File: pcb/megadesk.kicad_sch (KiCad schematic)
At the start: 24 parts, among them J1 Interface, J2 FFC, J3 AVR-ISP-6, U1 L7812, U2 L7805, U3 ATtiny841-SS, U4 MCP2003B

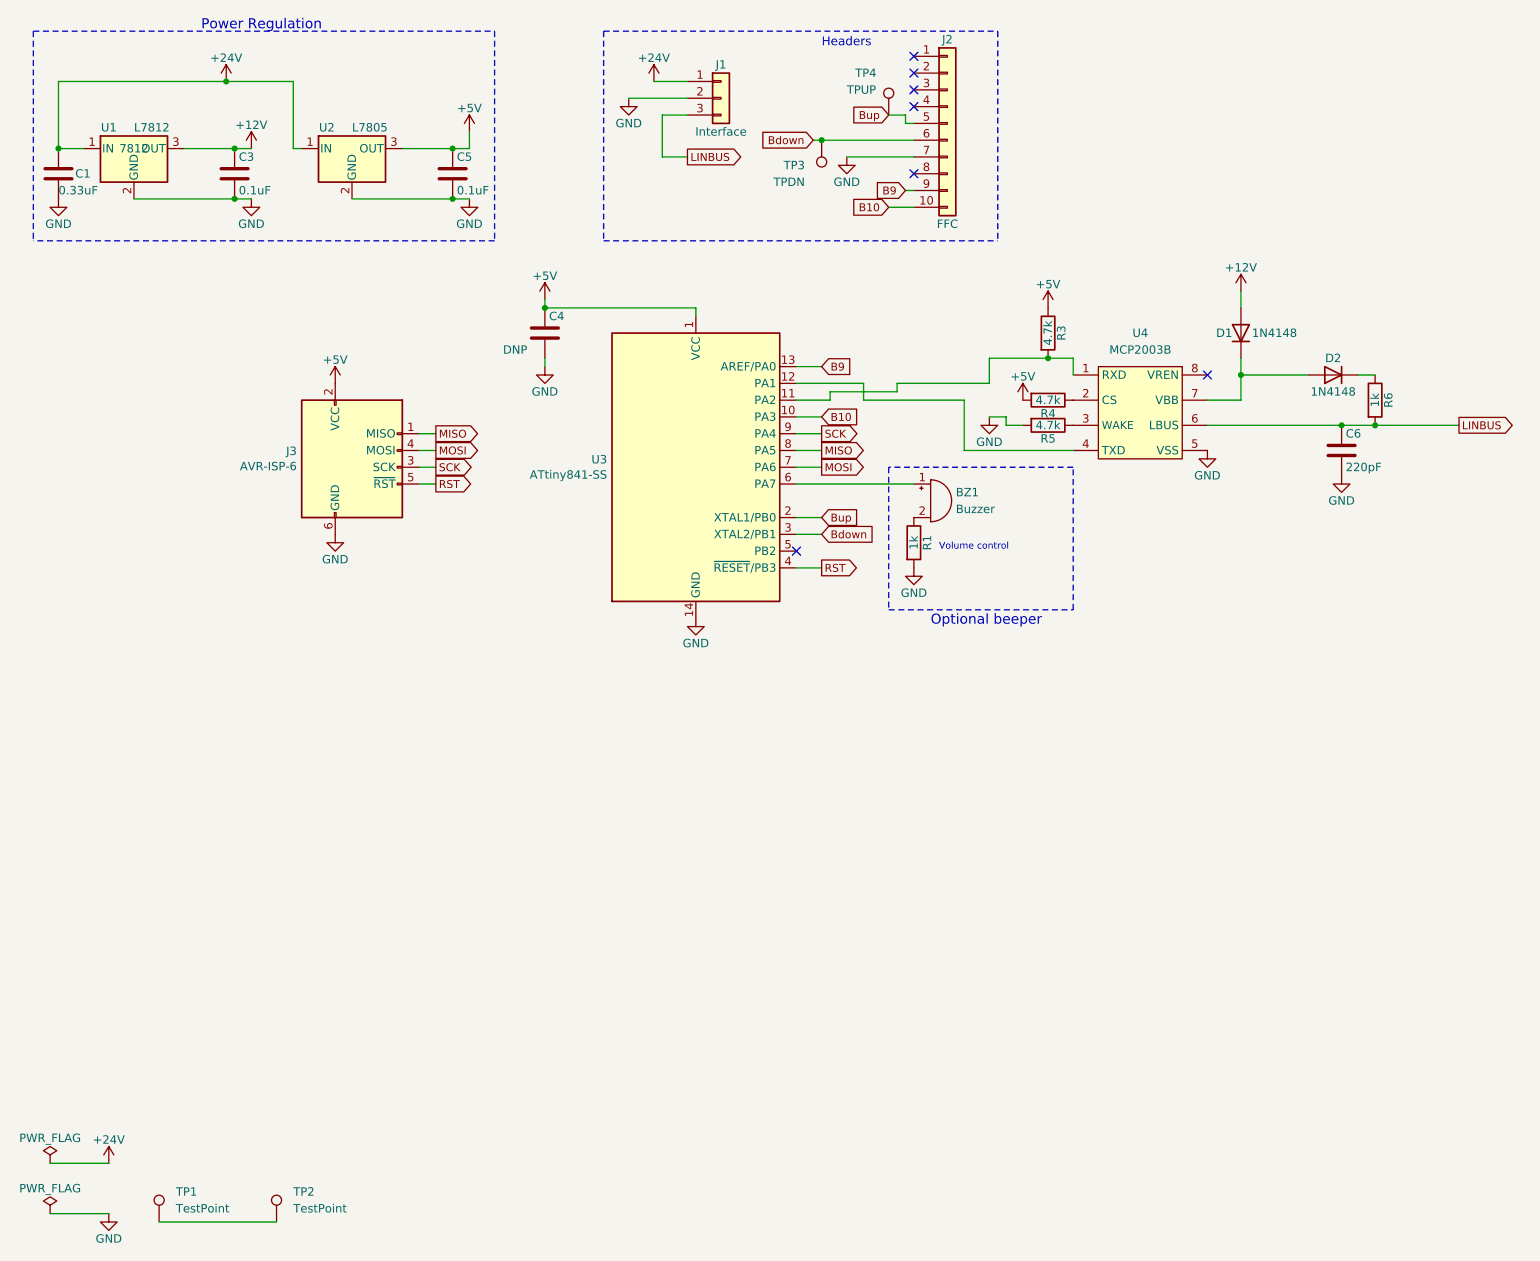
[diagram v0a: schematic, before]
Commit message: revise LDO's
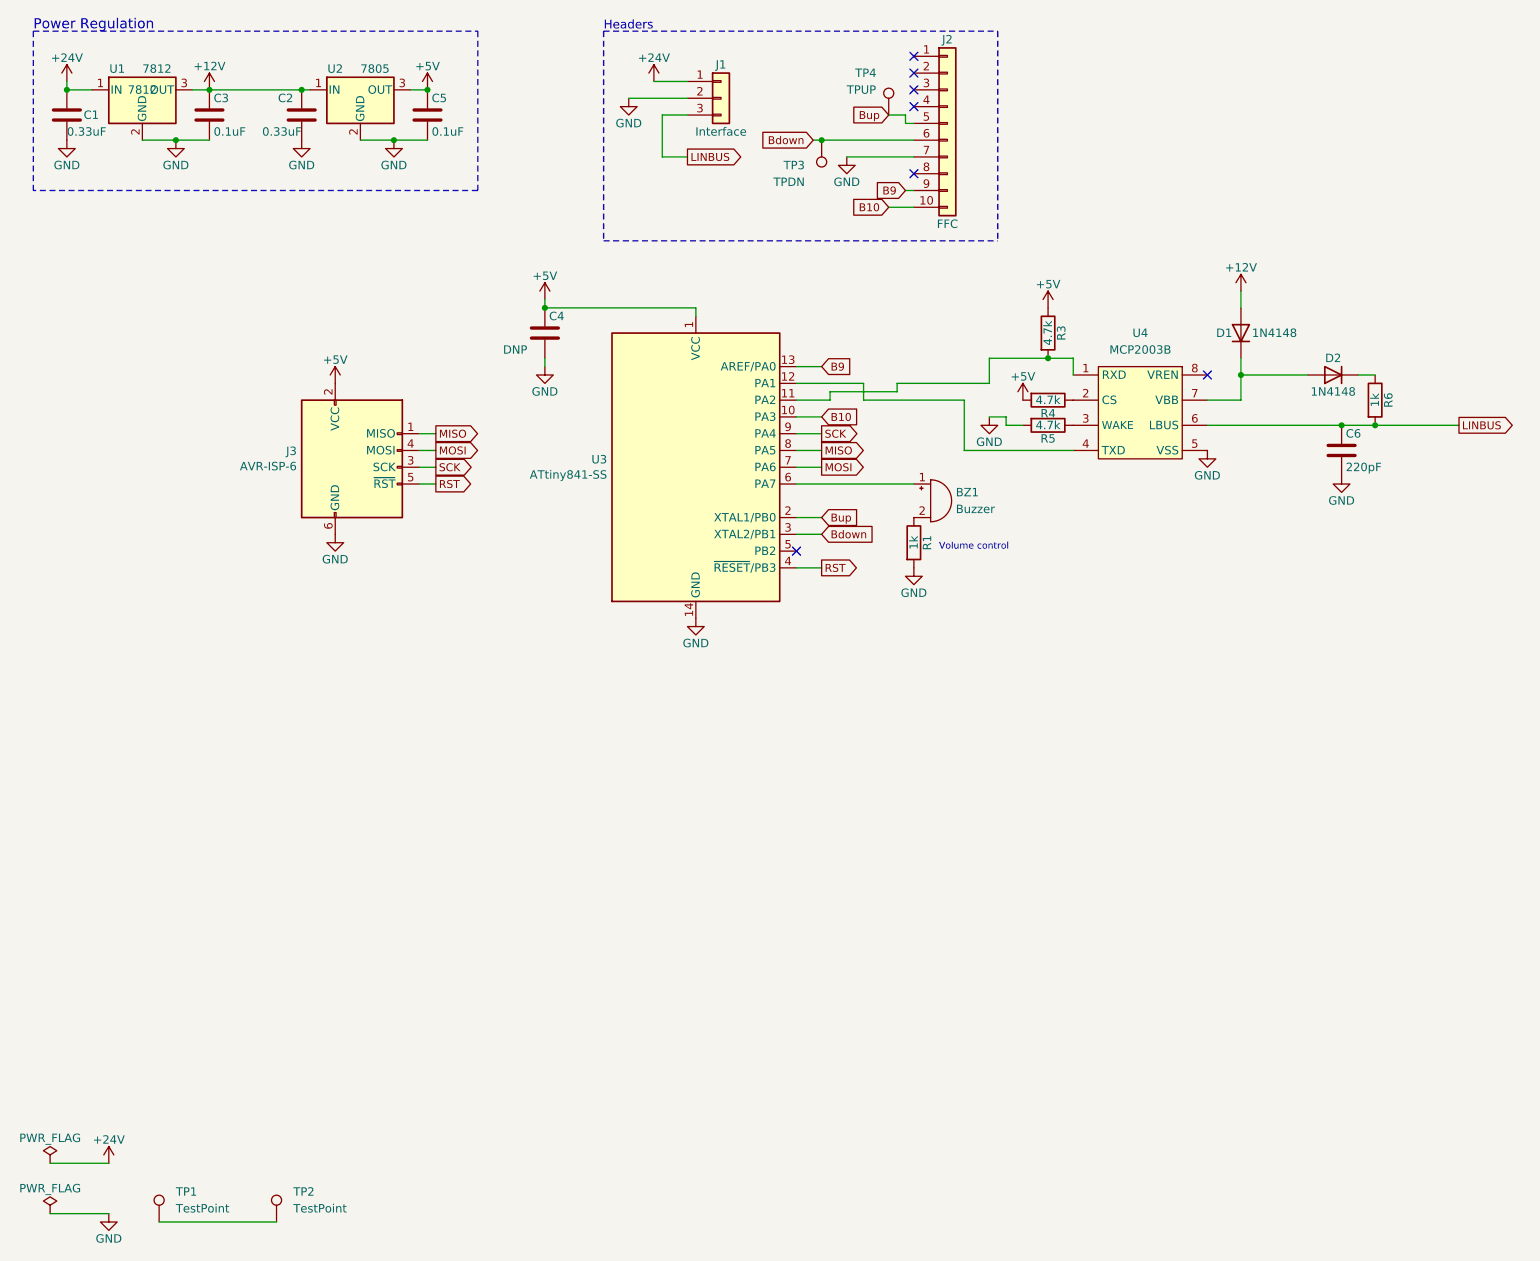
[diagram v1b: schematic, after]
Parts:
- added C2: 0.33uF, Capacitor_SMD:C_0805_2012Metric, symbol Device:C
- U1: value L7812 -> 7812; LCSC C16424 -> C116325; LCSC_ALT (none) -> C347282; Notes C16424 -> (none)
- U2: value L7805 -> 7805; footprint Package_TO_SOT_SMD:TO-252-3_TabPin2 -> Package_TO_SOT_SMD:SOT-89-3; LCSC C55509 -> C16106; Notes 35V INPUT -> (none); Part Number 7805 -> HT7550-1
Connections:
- net +12V: now also U2.1 (IN), C2.1
- net +24V: no longer U2.1 (IN)
- net GND: now also C2.2
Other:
- note removed: "Optional beeper"
- moved on the sheet: C1, C3, C5, U1, U2

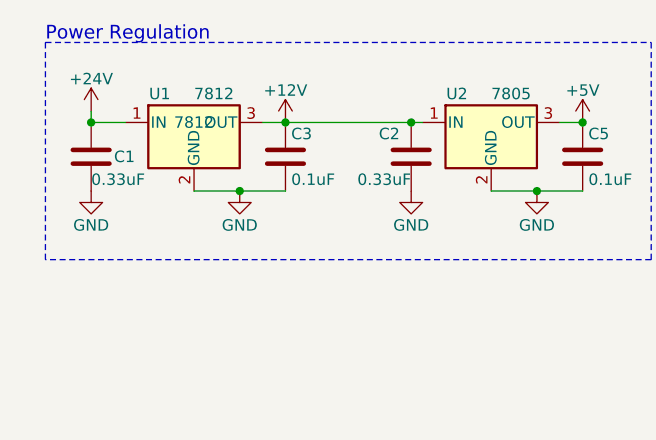
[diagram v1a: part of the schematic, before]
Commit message: simplify caps
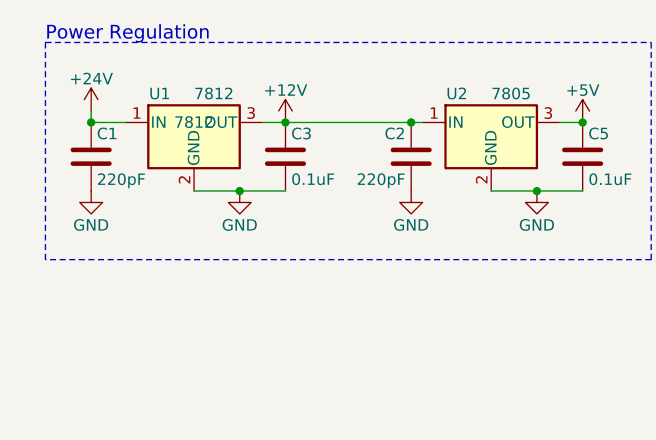
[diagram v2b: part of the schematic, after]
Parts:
- C1, C2: value 0.33uF -> 220pF; footprint Capacitor_SMD:C_0805_2012Metric -> Capacitor_SMD:C_0603_1608Metric; LCSC C1740 -> C1603

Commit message: ugh. fix bad pins.
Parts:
- removed U2: 7805, Package_TO_SOT_SMD:SOT-89-3, symbol Regulator_Linear:L7805
- added U2: HT7550-1, Package_TO_SOT_SMD:SOT-89-3, symbol Regulator_Linear:MCP1700-2502E_SOT89
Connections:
- net +12V: now also U2.2 (VI)
- net +5V: now also U2.3 (VO)
- net GND: now also U2.1 (GND)
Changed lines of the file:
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@@
     (pin "1")
-  )
-  (symbol (lib_id "Regulator_Linear:L7805") (at 64.77 26.67 0) (unit 1)
-    (in_bom yes) (on_board yes)
-    (property "Reference" "U2" (id 0) (at 60.96 23.495 0))
-    (property "Value" "7805" (id 1) (at 64.77 23.495 0)
-      (effects (font (size 1.27 1.27)) (justify left))
-    )
-    (property "Footprint" "Package_TO_SOT_SMD:SOT-89-3" (id 2) (at 65.405 30.48 0)
-      (effects (font (size 1.27 1.27) italic) (justify left) hide)
-    )
-    (property "Datasheet" "" (id 3) (at 64.77 27.94 0)
-      (effects (font (size 1.27 1.27)) hide)
-    )
-    (property "Part Number" "HT7550-1" (id 4) (at 64.77 26.67 0)
-      (effects (font (size 1.27 1.27)) hide)
-    )
-    (property "LCSC" "C16106" (id 5) (at 64.77 26.67 0)
-      (effects (font (size 1.27 1.27)) hide)
-    )
-    (property "Notes" "" (id 6) (at 64.77 26.67 0)
-      (effects (font (size 1.27 1.27)) hide)
-    )
-    (pin "1")
-    (pin "2")
-    (pin "3")
   )
   (symbol (lib_id "power:GND") (at 69.85 34.29 0) (unit 1)
@@
     (pin "1")
   )
+  (symbol (lib_id "Regulator_Linear:MCP1700-2502E_SOT89") (at 64.77 26.67 0) (unit 1)
+    (in_bom yes) (on_board yes) (fields_autoplaced)
+    (property "Reference" "U2" (id 0) (at 64.77 20.32 0))
+    (property "Value" "HT7550-1" (id 1) (at 64.77 22.86 0))
+    (property "Footprint" "Package_TO_SOT_SMD:SOT-89-3" (id 2) (at 64.77 21.59 0)
+      (effects (font (size 1.27 1.27)) hide)
+    )
+    (property "Datasheet" "https://datasheet.lcsc.com/lcsc/1811061932_Holtek-Semicon-HT7550-1_C16106.pdf" (id 3) (at 64.77 27.94 0)
+      (effects (font (size 1.27 1.27)) hide)
+    )
+    (property "LCSC" "C16106" (id 4) (at 64.77 26.67 0)
+      (effects (font (size 1.27 1.27)) hide)
+    )
+    (pin "1")
+    (pin "2")
+    (pin "3")
+  )
   (symbol (lib_id "power:GND") (at 55.88 34.29 0) (unit 1)
     (in_bom yes) (on_board yes)
@@
       (reference "U1") (unit 1) (value "7812") (footprint "Package_TO_SOT_SMD:TO-252-3_TabPin2")
     )
-    (path "/00000000-0000-0000-0000-00005a824df3"
-      (reference "U2") (unit 1) (value "7805") (footprint "Package_TO_SOT_SMD:SOT-89-3")
+    (path "/90a90260-d7e1-4930-8afc-9443a72d2d4b"
+      (reference "U2") (unit 1) (value "HT7550-1") (footprint "Package_TO_SOT_SMD:SOT-89-3")
     )
     (path "/00000000-0000-0000-0000-00005f8d16d9"

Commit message: kicad v7
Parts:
- U2: symbol Regulator_Linear:MCP1700-2502E_SOT89 -> Regulator_Linear:MCP1700x-120xxMB

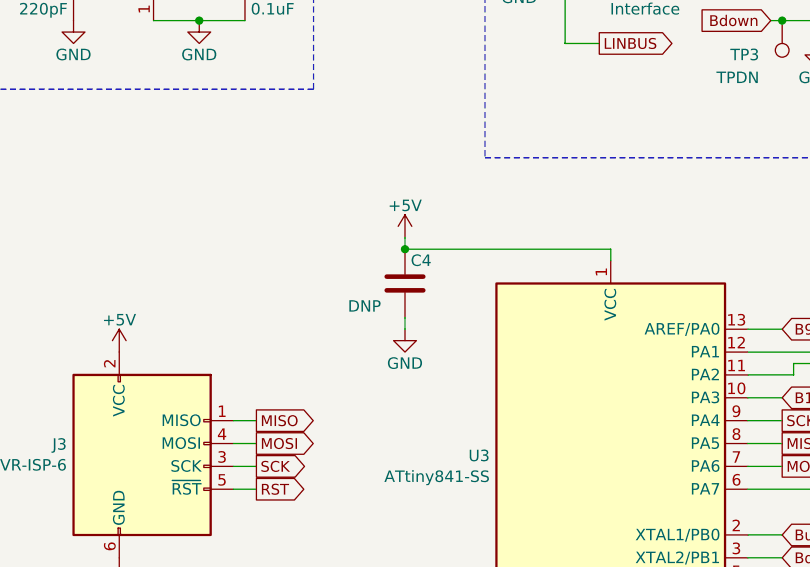
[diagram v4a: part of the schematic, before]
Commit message: fix silkscreen kibot and v7
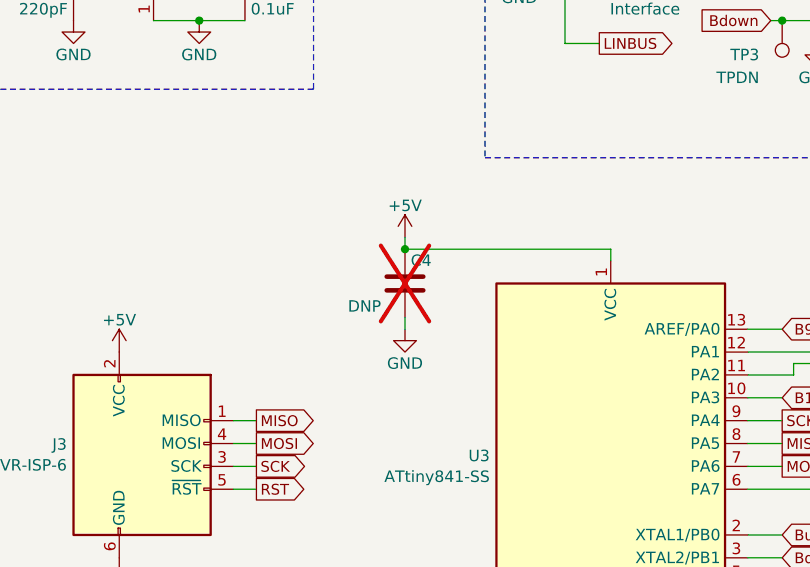
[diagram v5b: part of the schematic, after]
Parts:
- C4: now not fitted
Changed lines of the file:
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@@
   )
   (symbol (lib_id "Device:C") (at 92.71 63.5 0) (unit 1)
-    (in_bom yes) (on_board no) (dnp no)
+    (in_bom yes) (on_board no) (dnp yes)
     (property "Reference" "C4" (at 93.345 60.96 0)
       (effects (font (size 1.27 1.27)) (justify left))

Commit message: update PN for header
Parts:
- J1: LCSC C376121 -> C492411
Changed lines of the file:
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@@
       (effects (font (size 1.27 1.27)) hide)
     )
-    (property "LCSC" "C376121" (at 119.38 27.94 0)
+    (property "LCSC" "C492411" (at 119.38 27.94 0)
       (effects (font (size 1.27 1.27)) hide)
     )

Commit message: add PN's for ic
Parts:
- U3: LCSC DNP -> ATTINY841-SSUR; Part Number ATTINY841-SSURTR -> ATTINY841-SSUR
- U4: LCSC (none) -> MCP2003B-E/SN
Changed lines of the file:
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@@
       (effects (font (size 1.27 1.27)) hide)
     )
-    (property "LCSC" "DNP" (at 115.57 83.82 0)
+    (property "LCSC" "ATTINY841-SSUR" (at 115.57 83.82 0)
       (effects (font (size 1.27 1.27)) hide)
     )
-    (property "Part Number" "ATTINY841-SSURTR" (at 115.57 83.82 0)
+    (property "Part Number" "ATTINY841-SSUR" (at 115.57 83.82 0)
       (effects (font (size 1.27 1.27)) hide)
     )
@@
       (effects (font (size 1.27 1.27)) hide)
     )
-    (property "LCSC" "" (at 182.88 74.93 0)
+    (property "LCSC" "MCP2003B-E/SN" (at 182.88 74.93 0)
       (effects (font (size 1.27 1.27)) hide)
     )

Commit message: update panel regex
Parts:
- C4: LCSC DNP -> (none)
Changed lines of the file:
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@@
       (effects (font (size 1.27 1.27)) hide)
     )
-    (property "LCSC" "DNP" (at 92.71 63.5 0)
+    (property "LCSC" "" (at 92.71 63.5 0)
       (effects (font (size 1.27 1.27)) hide)
     )
